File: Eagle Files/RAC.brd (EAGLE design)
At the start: 100 x 78.7 mm, 9 parts

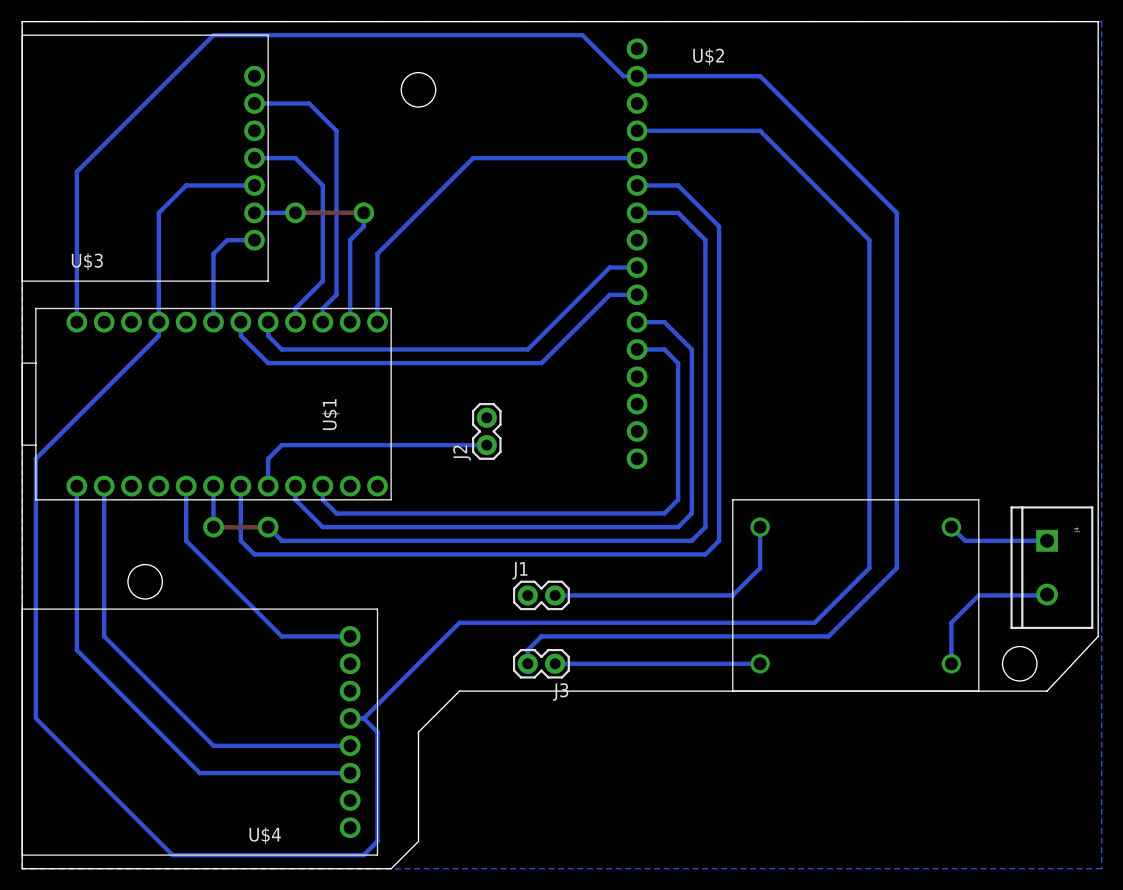
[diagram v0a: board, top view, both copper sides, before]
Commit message: Corrige error en regulador, amplía pads
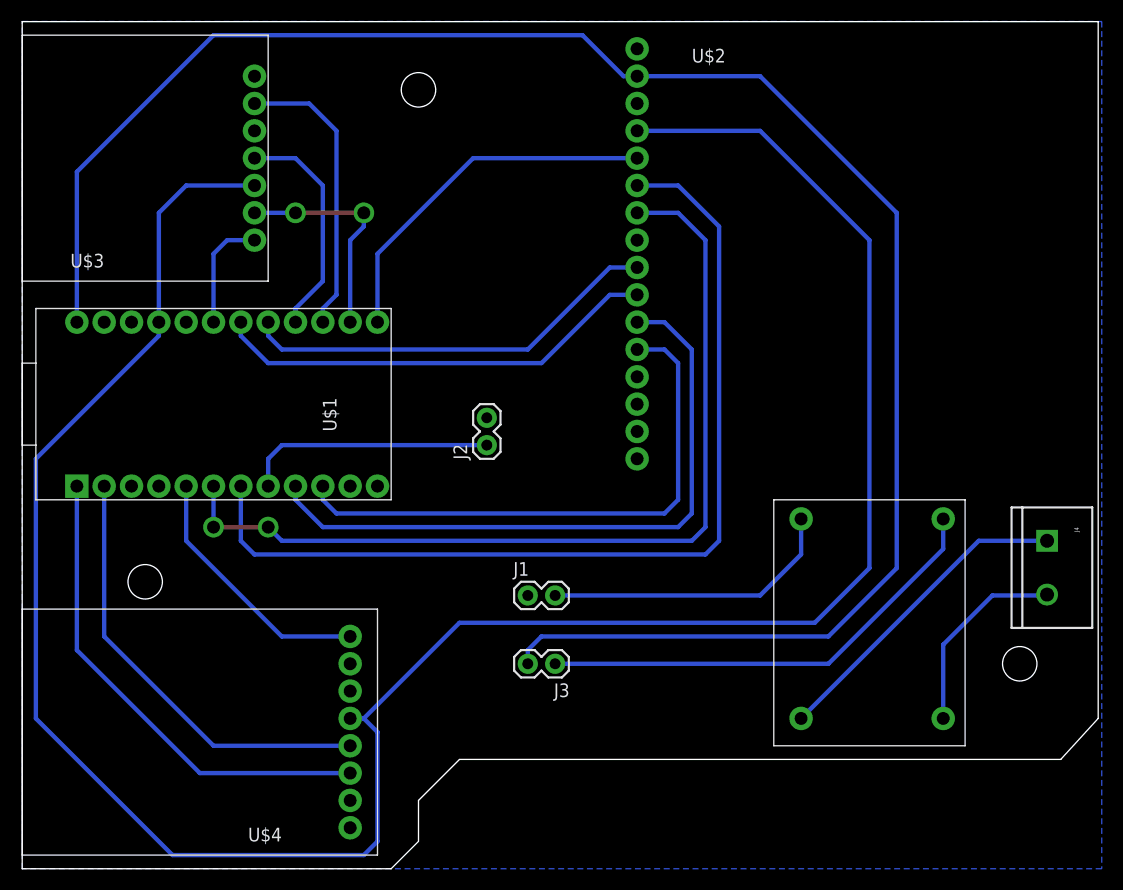
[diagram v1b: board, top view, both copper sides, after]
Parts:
- moved U$5 7.73 mm to (78.7, 24.1), turned to 90 degrees
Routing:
- net N$20: track 19.0 -> 43.3 mm
- net N$23: track 9.42 -> 29.7 mm
- net N$22: track 13.8 -> 18.4 mm
- net N$21: track 23.9 -> 27.7 mm
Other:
- outline, holes or cut-outs redrawn
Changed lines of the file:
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@@
 <setting verticaltext="up"/>
 </settings>
-<grid distance="0.05" unitdist="inch" unit="inch" style="lines" multiple="1" display="no" altdistance="0.025" altunitdist="inch" altunit="inch"/>
+<grid distance="0.05" unitdist="inch" unit="mm" style="lines" multiple="1" display="no" altdistance="0.025" altunitdist="inch" altunit="mm"/>
 <layers>
 <layer number="1" name="Top" color="4" fill="1" visible="yes" active="yes"/>
@@
 <wire x1="0" y1="1.27" x2="34.29" y2="1.27" width="0" layer="20"/>
 <wire x1="34.29" y1="1.27" x2="36.83" y2="3.81" width="0" layer="20"/>
-<wire x1="36.83" y1="3.81" x2="36.83" y2="13.97" width="0" layer="20"/>
-<wire x1="36.83" y1="13.97" x2="40.64" y2="17.78" width="0" layer="20"/>
-<wire x1="40.64" y1="17.78" x2="95.25" y2="17.78" width="0" layer="20"/>
-<wire x1="95.25" y1="17.78" x2="100" y2="22.86" width="0" layer="20"/>
-<wire x1="100" y1="22.86" x2="100" y2="80" width="0" layer="20"/>
+<wire x1="36.83" y1="3.81" x2="36.83" y2="7.62" width="0" layer="20"/>
+<wire x1="36.83" y1="7.62" x2="40.64" y2="11.43" width="0" layer="20"/>
+<wire x1="40.64" y1="11.43" x2="96.52" y2="11.43" width="0" layer="20"/>
+<wire x1="96.52" y1="11.43" x2="100" y2="15.24" width="0" layer="20"/>
+<wire x1="100" y1="15.24" x2="100" y2="80" width="0" layer="20"/>
 <wire x1="100" y1="80" x2="0" y2="80" width="0" layer="20"/>
 <wire x1="0" y1="80" x2="0" y2="1.27" width="0" layer="20"/>
@@
 <element name="U$3" library="rac" package="SD_BR" value="SD'A'" x="16.51" y="69.85" rot="R180"/>
 <element name="U$4" library="rac" package="BLE" value="BT_UART'A'" x="26.67" y="15.24" rot="R180"/>
-<element name="U$5" library="rac" package="DC-DC" value="DC-DC'A'" x="77.47" y="31.75" rot="R180"/>
+<element name="U$5" library="rac" package="DC-DC" value="DC-DC'A'" x="78.74" y="24.13" rot="R90"/>
 <element name="J4" library="SparkFun-Connectors" package="SCREWTERMINAL-5MM-2" value="" x="95.25" y="31.75" rot="R270">
 <attribute name="STOREFRONT_ID" value="PRT-08432" x="95.25" y="31.75" size="1.778" layer="27" rot="R270" display="off"/>
@@
 <contactref element="U$5" pad="OUT+"/>
 <contactref element="J3" pad="1"/>
-<wire x1="68.58" y1="20.32" x2="49.53" y2="20.32" width="0.4064" layer="16"/>
+<wire x1="85.598" y1="33.782" x2="85.598" y2="30.988" width="0.4064" layer="16"/>
+<wire x1="85.598" y1="30.988" x2="74.93" y2="20.32" width="0.4064" layer="16"/>
+<wire x1="74.93" y1="20.32" x2="49.53" y2="20.32" width="0.4064" layer="16"/>
 </signal>
 <signal name="N$21">
 <contactref element="U$5" pad="OUT-"/>
 <contactref element="J1" pad="2"/>
-<wire x1="49.53" y1="26.67" x2="66.04" y2="26.67" width="0.4064" layer="16"/>
-<wire x1="66.04" y1="26.67" x2="68.58" y2="29.21" width="0.4064" layer="16"/>
-<wire x1="68.58" y1="29.21" x2="68.58" y2="33.02" width="0.4064" layer="16"/>
+<wire x1="49.53" y1="26.67" x2="68.58" y2="26.67" width="0.4064" layer="16"/>
+<wire x1="68.58" y1="26.67" x2="72.39" y2="30.48" width="0.4064" layer="16"/>
+<wire x1="72.39" y1="30.48" x2="72.39" y2="33.782" width="0.4064" layer="16"/>
 </signal>
 <signal name="N$22">
 <contactref element="U$5" pad="IN+"/>
 <contactref element="J4" pad="2"/>
-<wire x1="86.36" y1="20.32" x2="86.36" y2="24.13" width="0.4064" layer="16"/>
-<wire x1="86.36" y1="24.13" x2="88.9" y2="26.67" width="0.4064" layer="16"/>
-<wire x1="88.9" y1="26.67" x2="95.17" y2="26.67" width="0.4064" layer="16"/>
+<wire x1="85.598" y1="15.24" x2="85.598" y2="22.098" width="0.4064" layer="16"/>
+<wire x1="85.598" y1="22.098" x2="90.17" y2="26.67" width="0.4064" layer="16"/>
+<wire x1="90.17" y1="26.67" x2="95.17" y2="26.67" width="0.4064" layer="16"/>
 <wire x1="95.17" y1="26.67" x2="95.25" y2="26.75" width="0.4064" layer="16"/>
 </signal>
@@
 <contactref element="U$5" pad="IN-"/>
 <contactref element="J4" pad="1"/>
-<wire x1="95.25" y1="31.75" x2="87.63" y2="31.75" width="0.4064" layer="16"/>
-<wire x1="87.63" y1="31.75" x2="86.36" y2="33.02" width="0.4064" layer="16"/>
+<wire x1="95.25" y1="31.75" x2="88.9" y2="31.75" width="0.4064" layer="16"/>
+<wire x1="72.39" y1="15.24" x2="88.9" y2="31.75" width="0.4064" layer="16"/>
 </signal>
 <signal name="S$1">
